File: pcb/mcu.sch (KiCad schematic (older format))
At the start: 29 parts, among them J1 Conn_02x10_Odd_Even, J2 Conn_01x03_Male, J3 Conn_01x04_Male, SW1 SW_Push, U1 STM32F407VGTx, Y1 32.768KHz, Y2 25MHz

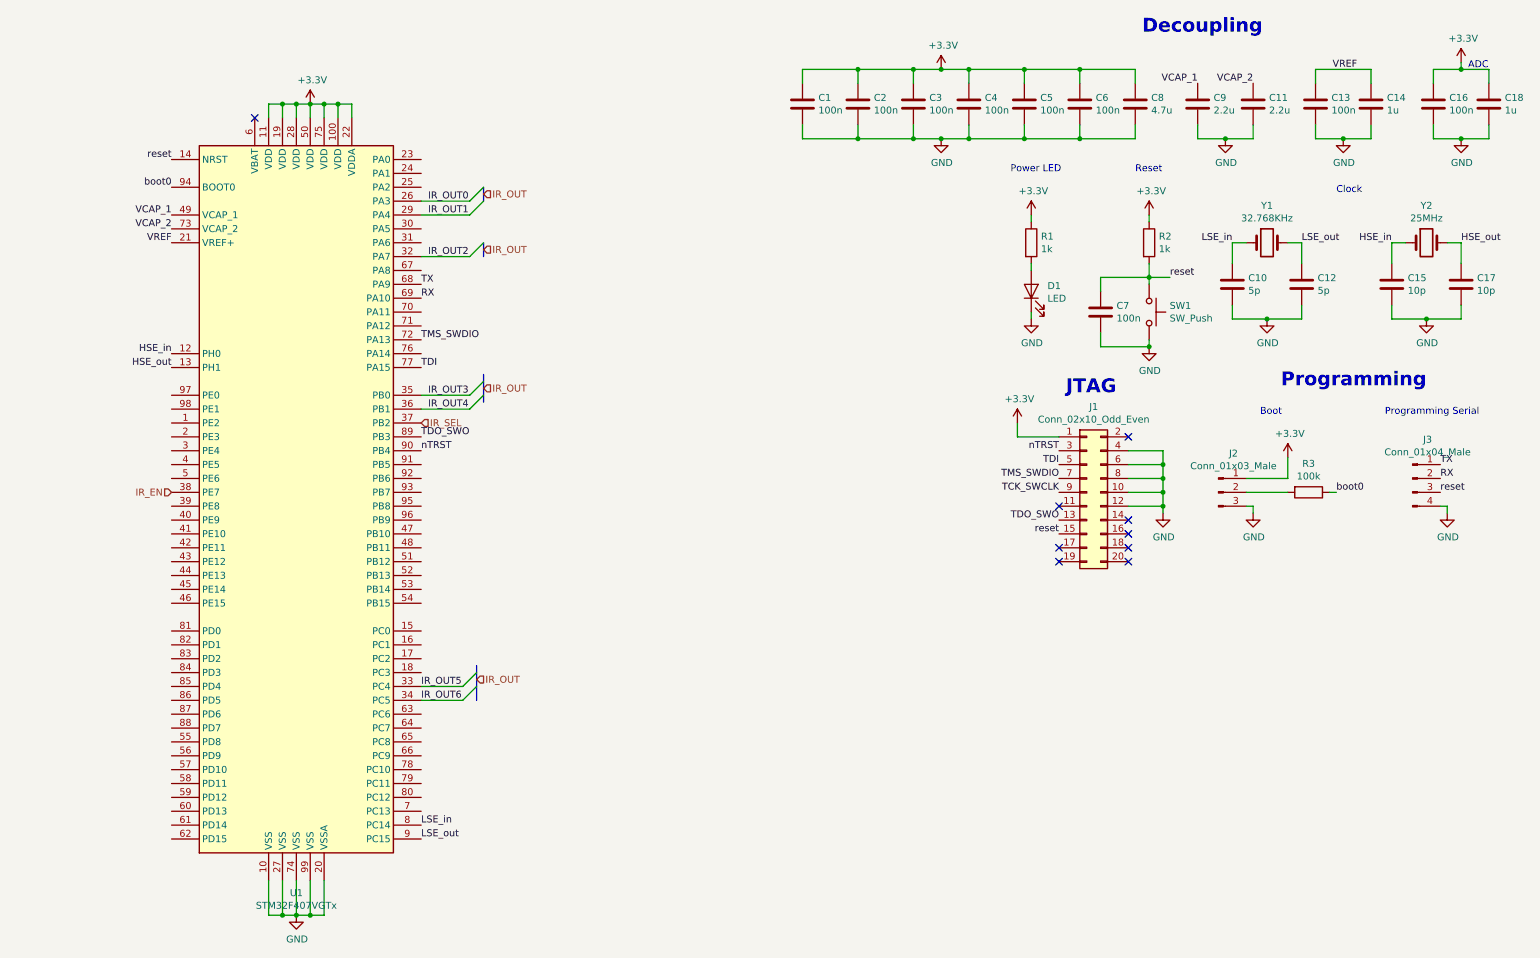
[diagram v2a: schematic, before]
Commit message: MCU connections, OLED and Sonar
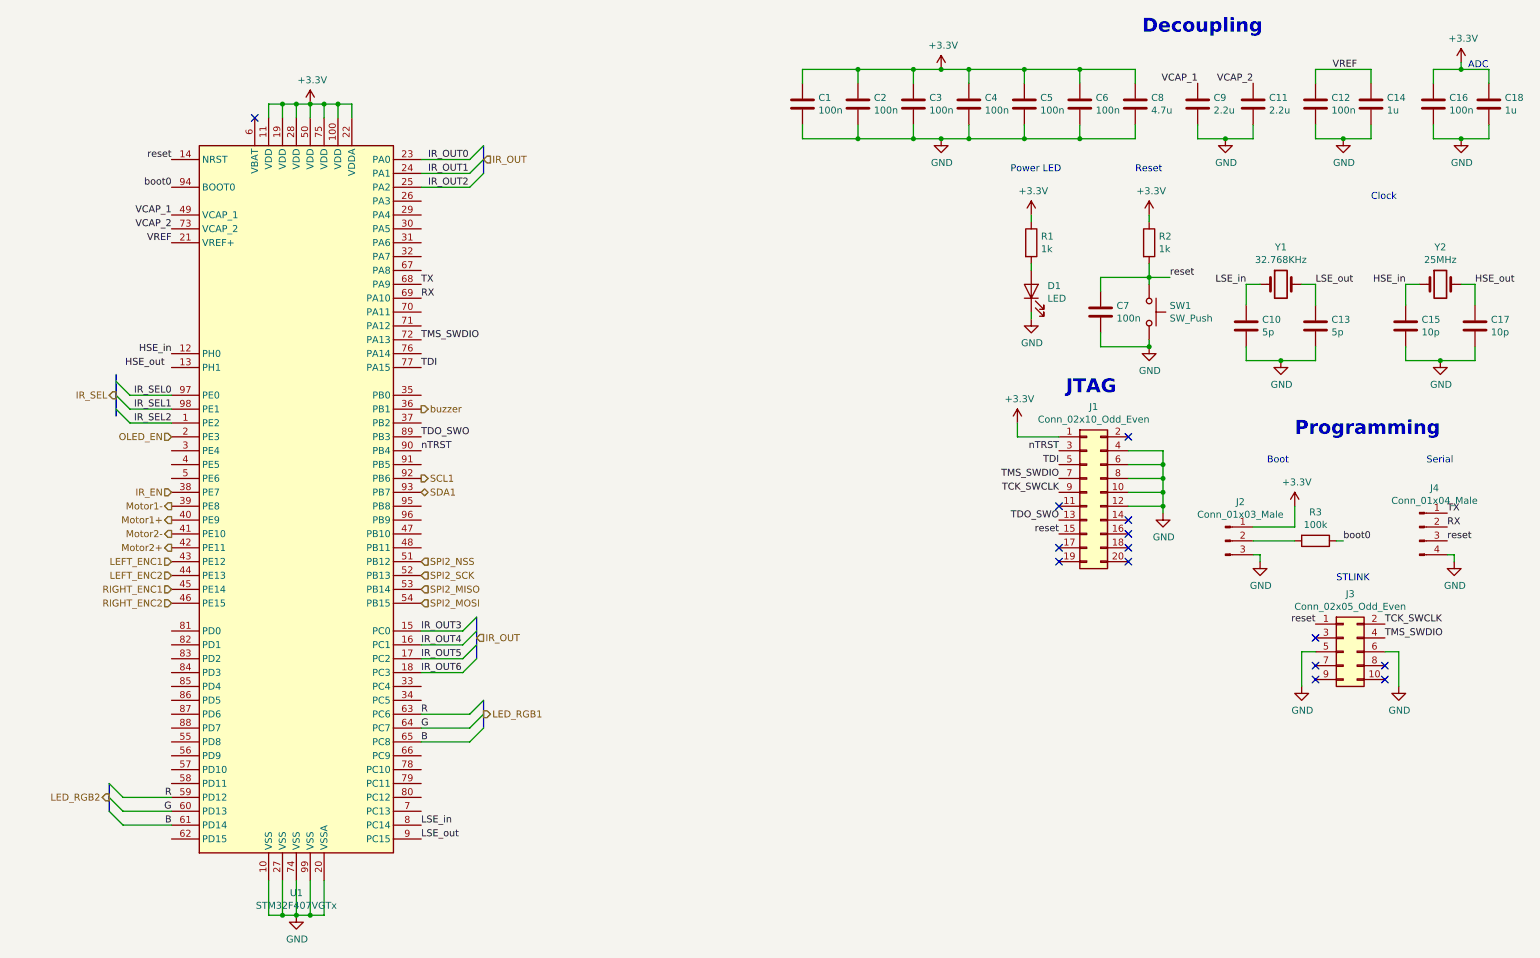
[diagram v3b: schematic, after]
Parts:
- added J3: Conn_02x05_Odd_Even, Connector_IDC:IDC-Header_2x05_P2.54mm_Vertical, symbol Connector_Generic:Conn_02x05_Odd_Even
- Y1: footprint Crystal:Crystal_SMD_SeikoEpson_MC306-4Pin_8.0x3.2mm -> Crystal:Crystal_SMD_2520-4Pin_2.5x2.0mm
- renumbered C13 to C12, C12 to C13, J3 to J4
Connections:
- net GND: now also J3.5 (Pin_5), J3.6 (Pin_6)
- net HSE_out: no longer U1.13 (PH1)
- net IR_OUT0: now also U1.23 (PA0); no longer U1.26 (PA3)
- net IR_OUT1: now also U1.24 (PA1); no longer U1.29 (PA4)
- net IR_OUT2: now also U1.25 (PA2); no longer U1.32 (PA7)
- net IR_OUT3: now also U1.15 (PC0); no longer U1.35 (PB0)
- net IR_OUT4: now also U1.16 (PC1); no longer U1.36 (PB1)
- net IR_OUT5: now also U1.17 (PC2); no longer U1.33 (PC4)
- net IR_OUT6: now also U1.18 (PC3); no longer U1.34 (PC5)
- net IR_SEL: no longer U1.37 (PB2)
- net TCK_SWCLK: now also J3.2 (Pin_2)
- net TMS_SWDIO: now also J3.4 (Pin_4)
- net reset: now also J3.1 (Pin_1)
- net IR_SEL2: now reaches U1.1 (PE2)
- net OLED_EN: now reaches U1.2 (PE3)
- net Motor1-: now reaches U1.39 (PE8)
- net Motor1+: now reaches U1.40 (PE9)
- net Motor2-: now reaches U1.41 (PE10)
- net Motor2+: now reaches U1.42 (PE11)
- net LEFT_ENC1: now reaches U1.43 (PE12)
- net LEFT_ENC2: now reaches U1.44 (PE13)
- net RIGHT_ENC1: now reaches U1.45 (PE14)
- net RIGHT_ENC2: now reaches U1.46 (PE15)
- net SPI2_NSS: now reaches U1.51 (PB12)
- net SPI2_SCK: now reaches U1.52 (PB13)
- net SPI2_MISO: now reaches U1.53 (PB14)
- net SPI2_MOSI: now reaches U1.54 (PB15)
- net R: now reaches U1.59 (PD12)
- net R: now also U1.63 (PC6)
- net G: now reaches U1.60 (PD13)
- net G: now also U1.64 (PC7)
- net B: now reaches U1.61 (PD14)
- net B: now also U1.65 (PC8)
- net SCL1: now reaches U1.92 (PB6)
- net SDA1: now reaches U1.93 (PB7)
- net IR_SEL0: now reaches U1.97 (PE0)
- net IR_SEL1: now reaches U1.98 (PE1)
- new net buzzer: U1.36 (PB1)
- no-connect marks 9 -> 14
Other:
- note added: "STLINK"
- note added: "Serial"
- note removed: "Programming Serial"
- moved on the sheet: C10, C13, C15, C17, J2, J4, R3, Y1, Y2

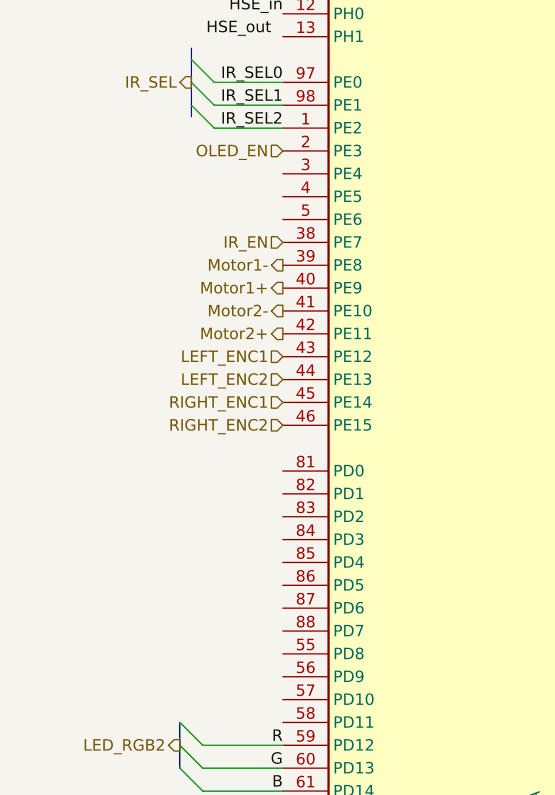
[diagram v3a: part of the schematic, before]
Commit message: Connect Ultrasonic Sensors
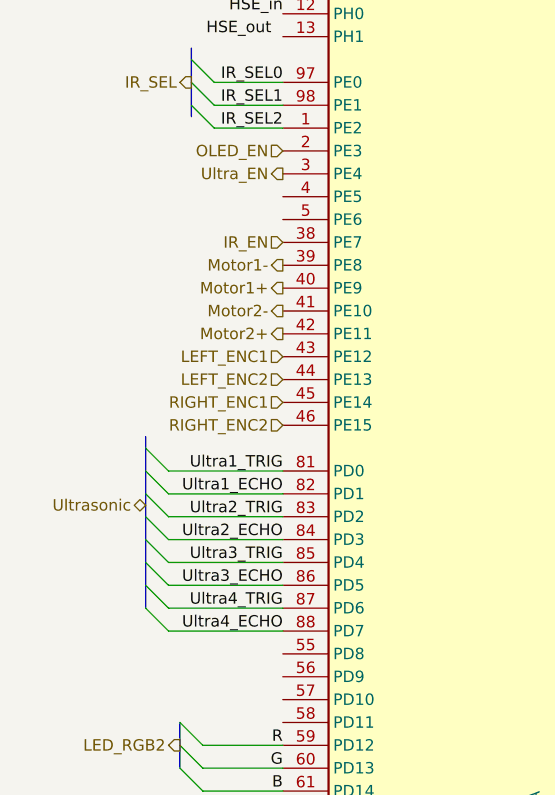
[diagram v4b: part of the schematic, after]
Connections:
- net Ultra_EN: now reaches U1.3 (PE4)
- net Ultra1_TRIG: now reaches U1.81 (PD0)
- net Ultra1_ECHO: now reaches U1.82 (PD1)
- net Ultra2_TRIG: now reaches U1.83 (PD2)
- net Ultra2_ECHO: now reaches U1.84 (PD3)
- net Ultra3_TRIG: now reaches U1.85 (PD4)
- net Ultra3_ECHO: now reaches U1.86 (PD5)
- net Ultra4_TRIG: now reaches U1.87 (PD6)
- net Ultra4_ECHO: now reaches U1.88 (PD7)
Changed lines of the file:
@@
 Wire Wire Line
 	1100 3550 1400 3550
+Text Label 1400 3450 2    50   ~ 0
+IR_SEL1
+Text Label 1400 3550 2    50   ~ 0
+IR_SEL2
+Text Label 1400 5650 2    50   ~ 0
+Ultra4_TRIG
+Text Label 1400 5750 2    50   ~ 0
+Ultra4_ECHO
+Text HLabel 800  5200 0    50   BiDi ~ 0
+Ultrasonic
+Entry Wire Line
+	800  4950 900  5050
+Entry Wire Line
+	800  5050 900  5150
+Entry Wire Line
+	800  5150 900  5250
+Entry Wire Line
+	800  5250 900  5350
+Entry Wire Line
+	800  5350 900  5450
+Entry Wire Line
+	800  5450 900  5550
+Entry Wire Line
+	800  5550 900  5650
+Entry Wire Line
+	800  5650 900  5750
+Wire Wire Line
+	900  5750 1400 5750
+Wire Wire Line
+	900  5650 1400 5650
+Wire Wire Line
+	900  5550 1400 5550
+Wire Wire Line
+	900  5450 1400 5450
+Wire Wire Line
+	1400 5350 900  5350
+Wire Wire Line
+	900  5250 1400 5250
+Wire Wire Line
+	1400 5150 900  5150
+Wire Wire Line
+	900  5050 1400 5050
 Wire Bus Line
 	950  6150 950  6350
@@
 Wire Bus Line
 	1000 3200 1000 3500
-Text Label 1400 3450 2    50   ~ 0
-IR_SEL1
-Text Label 1400 3550 2    50   ~ 0
-IR_SEL2
+Wire Bus Line
+	800  4900 800  5650
+Text Label 1400 5550 2    50   ~ 0
+Ultra3_ECHO
+Text Label 1400 5450 2    50   ~ 0
+Ultra3_TRIG
+Text Label 1400 5250 2    50   ~ 0
+Ultra2_TRIG
+Text Label 1400 5350 2    50   ~ 0
+Ultra2_ECHO
+Text Label 1400 5050 2    50   ~ 0
+Ultra1_TRIG
+Text Label 1400 5150 2    50   ~ 0
+Ultra1_ECHO
+Text HLabel 1400 3750 0    50   Output ~ 0
+Ultra_EN
 $EndSCHEMATC

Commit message: Rotary Encoder
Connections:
- net B: now also U1.71 (PA12); no longer U1.65 (PC8)
- net G: now also U1.70 (PA11); no longer U1.64 (PC7)
- net R: now also U1.62 (PD15); no longer U1.63 (PC6)
- net Rotary_DT: now reaches U1.4 (PE5)
- net Rotary_CLK: now reaches U1.5 (PE6)
- net Rotary_SW: now reaches U1.7 (PC13)
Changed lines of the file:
@@
 RIGHT_ENC2
 Entry Wire Line
-	3550 5650 3650 5550
-Entry Wire Line
-	3550 5850 3650 5750
-Entry Wire Line
-	3550 5750 3650 5650
-Text HLabel 3650 5650 2    50   Output ~ 0
+	1050 6550 950  6450
+Text HLabel 950  6500 0    50   Output ~ 0
 LED_RGB1
-Text Label 3200 5650 0    50   ~ 0
+Text Label 1400 6550 2    50   ~ 0
 R
-Text Label 3200 5750 0    50   ~ 0
-G
-Text Label 3200 5850 0    50   ~ 0
-B
-Wire Wire Line
-	3200 5650 3550 5650
-Wire Wire Line
-	3200 5750 3550 5750
-Wire Wire Line
-	3200 5850 3550 5850
+Wire Wire Line
+	1400 6550 1050 6550
 Wire Wire Line
 	3200 5150 3500 5150
@@
 Wire Wire Line
 	900  5050 1400 5050
-Wire Bus Line
-	950  6150 950  6350
-Wire Bus Line
-	3650 5550 3650 5750
-Wire Bus Line
-	3650 1550 3650 1750
-Wire Bus Line
-	3600 4950 3600 5250
-Wire Bus Line
-	1000 3200 1000 3500
-Wire Bus Line
-	800  4900 800  5650
 Text Label 1400 5550 2    50   ~ 0
 Ultra3_ECHO
@@
 Text HLabel 1400 3750 0    50   Output ~ 0
 Ultra_EN
+Entry Wire Line
+	3550 2850 3650 2750
+Entry Wire Line
+	3550 2750 3650 2650
+Text Label 3200 2750 0    50   ~ 0
+G
+Text Label 3200 2850 0    50   ~ 0
+B
+Wire Wire Line
+	3200 2750 3550 2750
+Wire Wire Line
+	3200 2850 3550 2850
+Text HLabel 3650 2700 2    50   Output ~ 0
+LED_RGB1
+Wire Bus Line
+	950  6500 950  6450
+Wire Bus Line
+	950  6150 950  6350
+Wire Bus Line
+	3650 1550 3650 1750
+Wire Bus Line
+	3650 2600 3650 2750
+Wire Bus Line
+	3600 4950 3600 5250
+Wire Bus Line
+	1000 3200 1000 3500
+Wire Bus Line
+	800  4900 800  5650
+Text HLabel 1400 3850 0    50   Input ~ 0
+Rotary_DT
+Text HLabel 1400 3950 0    50   Input ~ 0
+Rotary_CLK
+Text HLabel 3200 6350 2    50   Input ~ 0
+Rotary_SW
 $EndSCHEMATC

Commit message: Fix pins
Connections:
- net SCL1 is gone; now on net TX: U1.92 (PB6)
- net SDA1 is gone; now on net RX: U1.93 (PB7)
- net B: now also U1.70 (PA11); no longer U1.71 (PA12)
- net G: now also U1.69 (PA10); no longer U1.70 (PA11)
- net RX: no longer U1.69 (PA10)
- net TX: no longer U1.68 (PA9)
- net SCL2: now reaches U1.47 (PB10)
- net SDA2: now reaches U1.48 (PB11)
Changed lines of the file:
@@
 Text Notes 9500 3650 0    100  ~ 20
 Programming
-Text Label 3200 2550 0    50   ~ 0
+Text Label 3200 3950 0    50   ~ 0
 TX
-Text Label 3200 2650 0    50   ~ 0
+Text Label 3200 4050 0    50   ~ 0
 RX
 $Comp
@@
 Wire Wire Line
 	3500 5050 3200 5050
-Text HLabel 3200 3950 2    50   Output ~ 0
-SCL1
-Text HLabel 3200 4050 2    50   BiDi ~ 0
-SDA1
+Text HLabel 3200 4350 2    50   Output ~ 0
+SCL2
+Text HLabel 3200 4450 2    50   BiDi ~ 0
+SDA2
 Text HLabel 3200 4650 2    50   Input ~ 0
 SPI2_SCK
@@
 Ultra_EN
 Entry Wire Line
-	3550 2850 3650 2750
-Entry Wire Line
 	3550 2750 3650 2650
+Entry Wire Line
+	3550 2650 3650 2550
+Text Label 3200 2650 0    50   ~ 0
+G
 Text Label 3200 2750 0    50   ~ 0
-G
-Text Label 3200 2850 0    50   ~ 0
 B
 Wire Wire Line
+	3200 2650 3550 2650
+Wire Wire Line
 	3200 2750 3550 2750
-Wire Wire Line
-	3200 2850 3550 2850
-Text HLabel 3650 2700 2    50   Output ~ 0
+Text HLabel 3650 2600 2    50   Output ~ 0
 LED_RGB1
 Wire Bus Line
 	950  6500 950  6450
+Text HLabel 1400 3850 0    50   Input ~ 0
+Rotary_DT
+Text HLabel 1400 3950 0    50   Input ~ 0
+Rotary_CLK
+Text HLabel 3200 6350 2    50   Input ~ 0
+Rotary_SW
 Wire Bus Line
 	950  6150 950  6350
@@
 	3650 1550 3650 1750
 Wire Bus Line
-	3650 2600 3650 2750
+	3650 2500 3650 2650
 Wire Bus Line
 	3600 4950 3600 5250
@@
 Wire Bus Line
 	800  4900 800  5650
-Text HLabel 1400 3850 0    50   Input ~ 0
-Rotary_DT
-Text HLabel 1400 3950 0    50   Input ~ 0
-Rotary_CLK
-Text HLabel 3200 6350 2    50   Input ~ 0
-Rotary_SW
 $EndSCHEMATC
